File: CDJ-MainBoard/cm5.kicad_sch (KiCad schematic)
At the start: 18 parts, among them J1 J_FAN_PWM, SW1 DSWB05LHGET, SW2 PWR_BUT_CM5, U1 Compute_Module_5_Functional

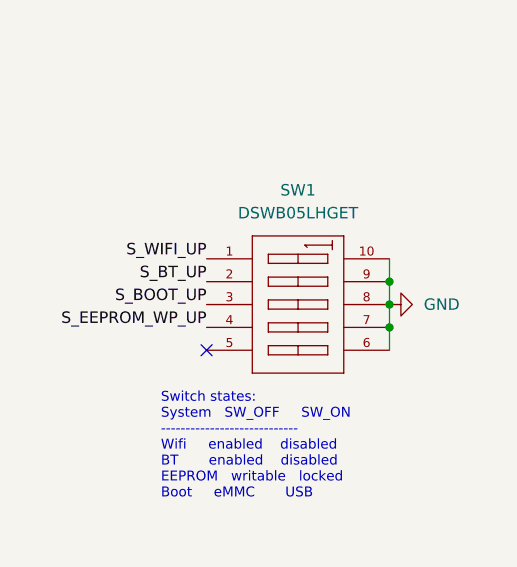
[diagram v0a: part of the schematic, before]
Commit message: Add connectors for sections of inputs, and list of all inputs in XLSX
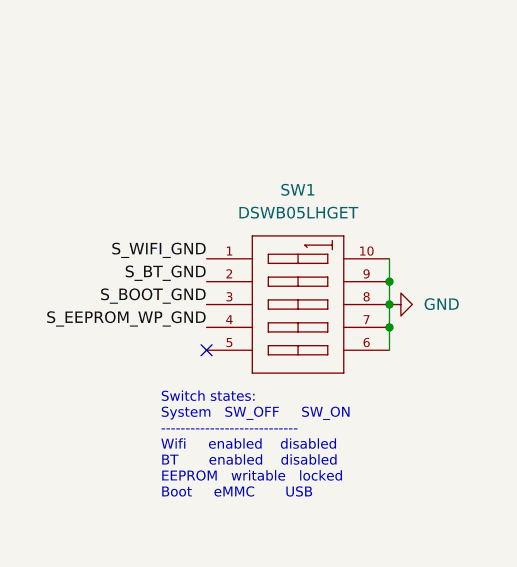
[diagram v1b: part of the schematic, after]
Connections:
- net S_BOOT_UP is gone; now on net S_BOOT_GND: SW1.3 (A3)
- net S_BT_UP is gone; now on net S_BT_GND: SW1.2 (A2)
- net S_EEPROM_WP_UP is gone; now on net S_EEPROM_WP_GND: SW1.4 (A4)
- net S_WIFI_UP is gone; now on net S_WIFI_GND: SW1.1 (A1)
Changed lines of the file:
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@@
 		)
 	)
-	(label "S_WIFI_UP"
+	(label "S_WIFI_GND"
 		(at 41.91 148.59 180)
 		(effects
@@
 		)
 	)
-	(label "S_BT_UP"
+	(label "S_BT_GND"
 		(at 41.91 151.13 180)
 		(effects
@@
 		)
 	)
-	(label "S_BOOT_UP"
+	(label "S_BOOT_GND"
 		(at 41.91 153.67 180)
 		(effects
@@
 		)
 	)
-	(label "S_EEPROM_WP_UP"
+	(label "S_EEPROM_WP_GND"
 		(at 41.91 156.21 180)
 		(effects

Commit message: Route SD card and misc
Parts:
- added C65, C66, C75: 100nF, PCM_JLCPCB:C_0402, symbol PCM_JLCPCB-Capacitors:0402,100nF
- added C76: 10uF, PCM_JLCPCB:C_0805, symbol PCM_JLCPCB-Capacitors:0805,10uF
- added Q1: AO3400A NFET, PCM_JLCPCB:Q_SOT-23, symbol PCM_JLCPCB-Transistors:NMOS,AO3400A
- added Q2: SI2301CDS-T1-GE3 P-FET, PCM_JLCPCB:Q_SOT-23, symbol PCM_JLCPCB-Transistors:PMOS,SI2301CDS-T1-GE3
- added R69: 33Ω, PCM_JLCPCB:R_0402, symbol PCM_JLCPCB-Resistors:0402,33Ω
- added R70, R71, R72, R73, R74, R75, R76: 10kΩ, PCM_JLCPCB:R_0402, symbol PCM_JLCPCB-Resistors:0402,10kΩ
- added unit 9 of U1
- added U20: TF-15×15, JLC2KiCad_lib-footprints:TF-SMD_TF-15-15, symbol TF-15×15:TF-15×15
- added U21, U23, U7: USBLC6-2SC6-ES, JLC2KiCad_lib-footprints:SOT-23-6_L2.9-W1.6-P0.95-LS2.8-BR, symbol jlc_USBLC6-2SC6-ES:USBLC6-2SC6-ES
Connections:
- net +3.3V: now also C65.1, C66.1, C75.1, Q2.2 (S), R70.1, R71.1, R72.1, R73.1, R74.1, R75.1, R76.1, U21.5 (VCC), U23.5 (VCC), U7.5 (VCC)
- net GND: now also C65.2, C66.2, C75.2, C76.1, Q1.2 (S), U20.10 (G3), U20.11 (G4), U20.12 (G1), U20.13 (G2), U20.6 (VSS), U21.2 (GND), U23.2 (GND), U7.2 (GND)
- new net: R69.1, U1.57 (SD_CLK)
- new net: Q1.3 (D), Q2.1 (G), R73.2
- new net SD_CLK: R69.2, U20.5 (CLK), U23.1 (I/O1), U23.6 (I/O1)
- new net SD_CMD: R70.2, U1.62 (SD_CMD), U20.3 (CMD), U23.3 (I/O2), U23.4 (I/O2)
- new net SD_DAT0: R76.2, U1.63 (SD_DAT0), U20.7 (DAT0), U7.1 (I/O1), U7.6 (I/O1)
- new net SD_DAT1: R75.2, U1.67 (SD_DAT1), U20.8 (DAT1), U7.3 (I/O2), U7.4 (I/O2)
- new net SD_DAT2: R74.2, U1.69 (SD_DAT2), U20.1 (DAT2), U21.3 (I/O2), U21.4 (I/O2)
- new net SD_DAT3: R72.2, U1.61 (SD_DAT3), U20.2 (CD/DAT3), U21.1 (I/O1), U21.6 (I/O1)
- new net SD_PWR_ON: Q1.1 (G), R71.2, U1.75 (SD_PWR_ON)
- new net SD_VDD: C76.2, Q2.3 (D), U20.4 (VDD)
- no-connect marks 26 -> 32
